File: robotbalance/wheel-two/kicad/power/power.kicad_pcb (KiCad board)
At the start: 2 copper layers, 55.9 x 35.6 mm, 0 parts

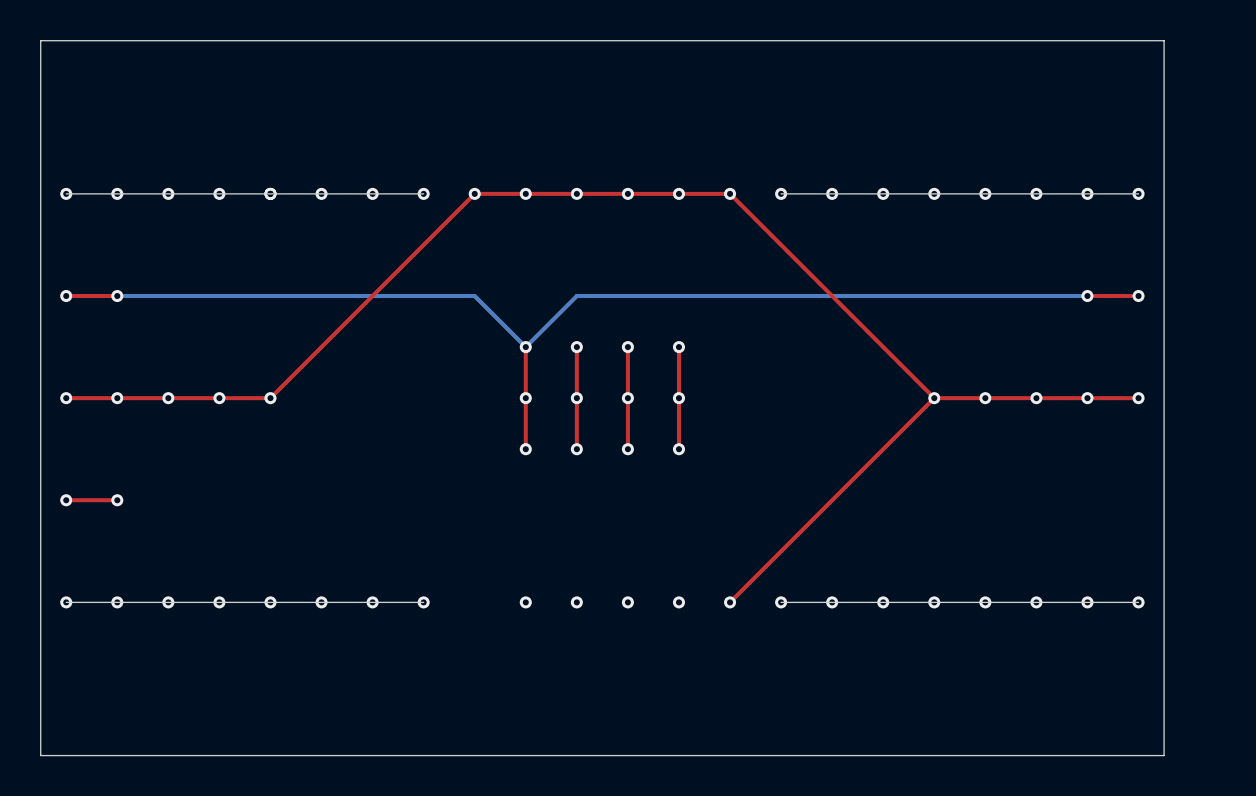
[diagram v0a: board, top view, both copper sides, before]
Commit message: balancing robot: 1.change pid in web in wifi 2.power board 3.another logic board esp32s3_weact+icm42688
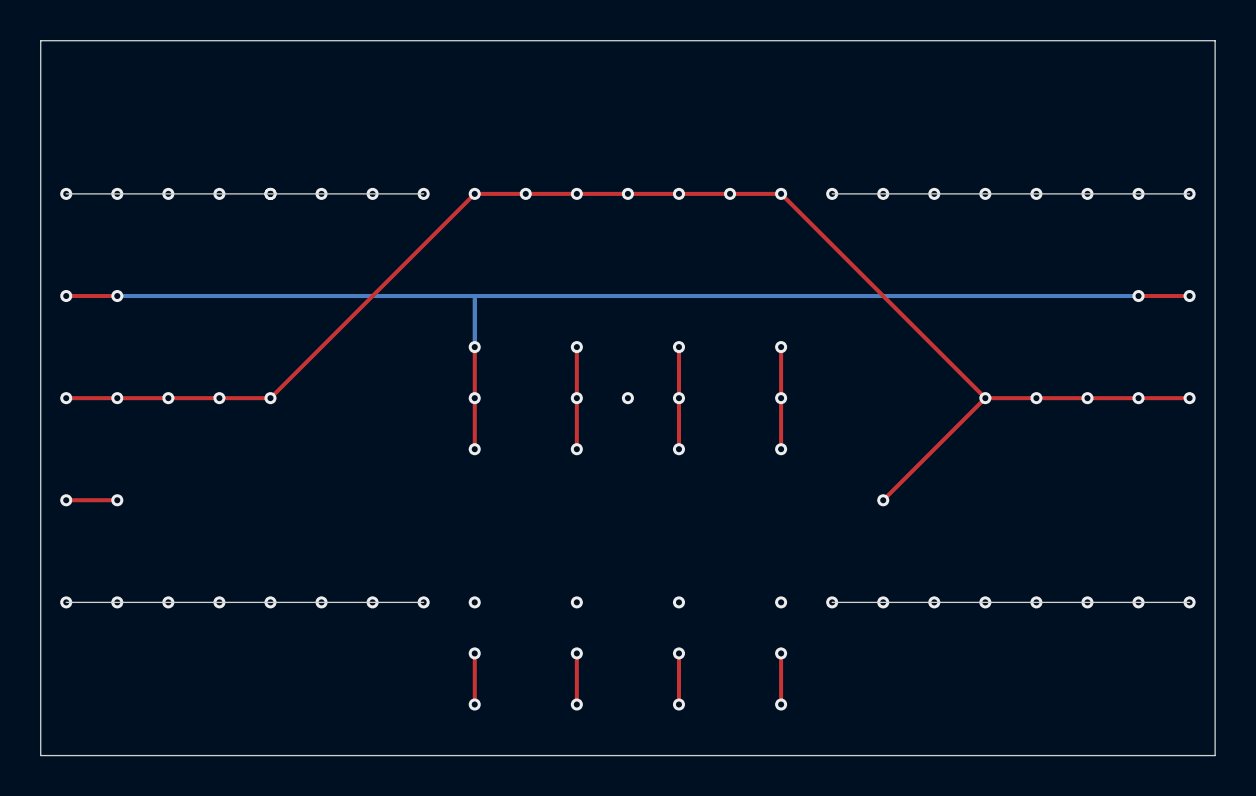
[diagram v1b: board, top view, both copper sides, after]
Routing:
- net (no net): track 154.4 -> 162.9 mm, vias 72 -> 82
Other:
- board size 55.9 x 35.6 mm -> 58.4 x 35.6 mm

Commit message: balancing robot: prepare for stepper motor
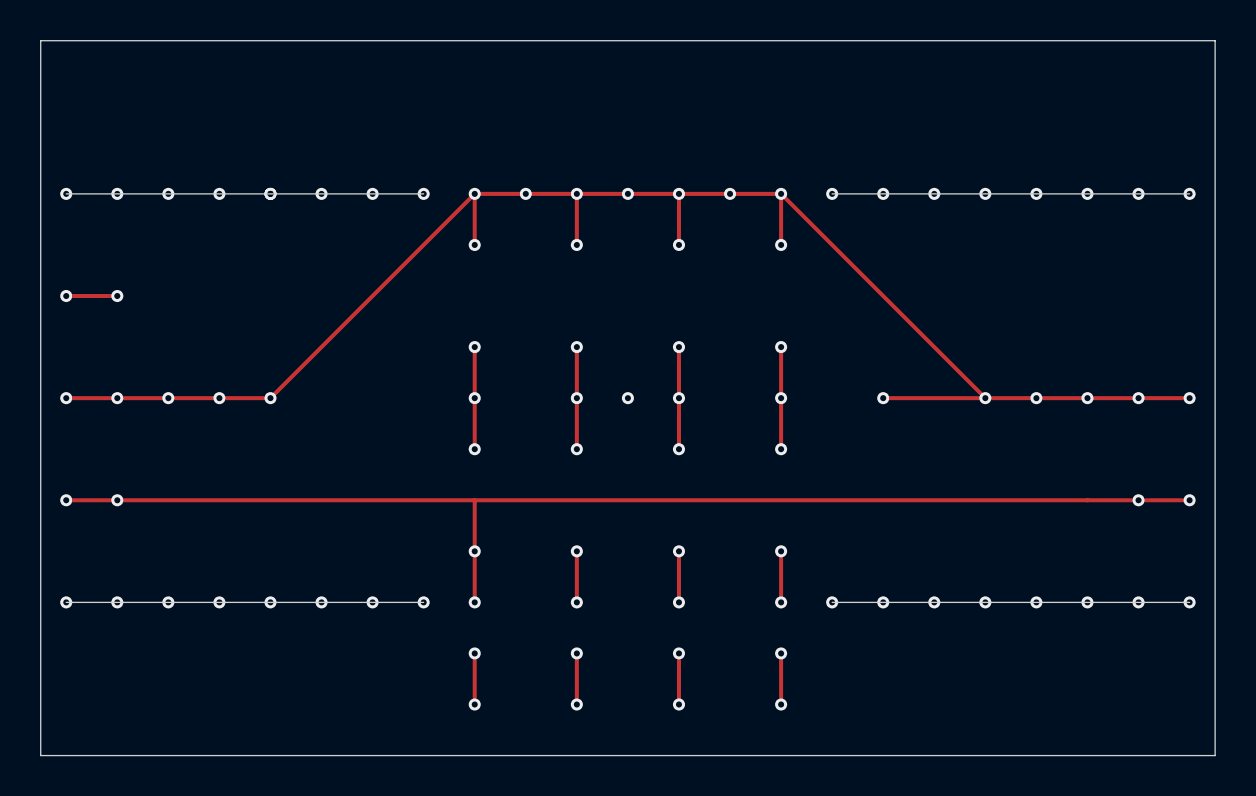
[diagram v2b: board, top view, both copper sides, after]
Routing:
- net (no net): track 162.9 -> 181.1 mm, vias 82 -> 90
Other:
- board text added: "gnd"
- board text removed: "0s"
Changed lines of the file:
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@@
 		)
 	)
-	(gr_text "4s"
-		(at 182.88 93.98 0)
-		(layer "Edge.Cuts")
-		(effects
-			(font
-				(size 1 1)
-				(thickness 0.15)
-			)
-			(justify right bottom)
-		)
-	)
-	(gr_text "0s"
-		(at 167.64 104.14 0)
+	(gr_text "gnd"
+		(at 167.64 99.06 0)
 		(layer "Edge.Cuts")
 		(effects
@@
 	)
 	(gr_text "4s"
-		(at 127 93.98 0)
+		(at 127 104.14 0)
 		(layer "Edge.Cuts")
 		(effects
@@
 	)
 	(gr_text "5v"
-		(at 127 104.14 0)
+		(at 127 93.98 0)
 		(layer "Edge.Cuts")
 		(effects
@@
 		)
 	)
+	(gr_text "4s"
+		(at 182.88 104.14 0)
+		(layer "Edge.Cuts")
+		(effects
+			(font
+				(size 1 1)
+				(thickness 0.15)
+			)
+			(justify right bottom)
+		)
+	)
 	(gr_text "3s"
 		(at 152.4 109.22 0)
@@
 	)
 	(segment
+		(start 162.56 106.68)
+		(end 162.56 109.22)
+		(width 0.2)
+		(layer "F.Cu")
+		(net 0)
+	)
+	(segment
+		(start 152.4 88.9)
+		(end 152.4 91.44)
+		(width 0.2)
+		(layer "F.Cu")
+		(net 0)
+	)
+	(segment
 		(start 147.32 88.9)
 		(end 137.16 99.06)
@@
 	)
 	(segment
+		(start 180.34 104.14)
+		(end 182.88 104.14)
+		(width 0.2)
+		(layer "F.Cu")
+		(net 0)
+	)
+	(segment
 		(start 172.72 99.06)
 		(end 175.26 99.06)
@@
 	)
 	(segment
+		(start 147.32 88.9)
+		(end 147.32 91.44)
+		(width 0.2)
+		(layer "F.Cu")
+		(net 0)
+	)
+	(segment
+		(start 147.32 104.14)
+		(end 147.32 106.68)
+		(width 0.2)
+		(layer "F.Cu")
+		(net 0)
+	)
+	(segment
+		(start 167.64 99.06)
+		(end 172.72 99.06)
+		(width 0.2)
+		(layer "F.Cu")
+		(net 0)
+	)
+	(segment
 		(start 157.48 111.76)
 		(end 157.48 114.3)
@@
 	)
 	(segment
+		(start 129.54 104.14)
+		(end 147.32 104.14)
+		(width 0.2)
+		(layer "F.Cu")
+		(net 0)
+	)
+	(segment
 		(start 134.62 99.06)
 		(end 132.08 99.06)
@@
 	)
 	(segment
+		(start 152.4 109.22)
+		(end 152.4 106.68)
+		(width 0.2)
+		(layer "F.Cu")
+		(net 0)
+	)
+	(segment
 		(start 152.4 111.76)
 		(end 152.4 114.3)
@@
 	)
 	(segment
-		(start 167.64 104.14)
-		(end 172.72 99.06)
-		(width 0.2)
-		(layer "F.Cu")
-		(net 0)
-	)
-	(segment
 		(start 180.34 99.06)
 		(end 182.88 99.06)
@@
 	)
 	(segment
+		(start 147.32 109.22)
+		(end 147.32 106.68)
+		(width 0.2)
+		(layer "F.Cu")
+		(net 0)
+	)
+	(segment
 		(start 149.86 88.9)
 		(end 147.32 88.9)
@@
 	)
 	(segment
-		(start 182.88 93.98)
-		(end 180.34 93.98)
+		(start 157.48 106.68)
+		(end 157.48 109.22)
 		(width 0.2)
 		(layer "F.Cu")
@@
 	)
 	(segment
+		(start 162.56 91.44)
+		(end 162.56 88.9)
+		(width 0.2)
+		(layer "F.Cu")
+		(net 0)
+	)
+	(segment
+		(start 147.32 104.14)
+		(end 177.8 104.14)
+		(width 0.2)
+		(layer "F.Cu")
+		(net 0)
+	)
+	(segment
 		(start 137.16 99.06)
 		(end 134.62 99.06)
@@
 	)
 	(segment
+		(start 157.48 91.44)
+		(end 157.48 88.9)
+		(width 0.2)
+		(layer "F.Cu")
+		(net 0)
+	)
+	(segment
+		(start 177.8 104.14)
+		(end 180.34 104.14)
+		(width 0.2)
+		(layer "F.Cu")
+		(net 0)
+	)
+	(segment
 		(start 172.72 99.06)
 		(end 162.56 88.9)
@@
 	)
 	(via
-		(at 167.64 104.14)
+		(at 167.64 99.06)
 		(size 0.6)
 		(drill 0.3)
@@
 	)
 	(via
+		(at 162.56 91.44)
+		(size 0.6)
+		(drill 0.3)
+		(layers "F.Cu" "B.Cu")
+		(net 0)
+	)
+	(via
 		(at 157.48 109.22)
 		(size 0.6)
@@
 	)
 	(via
+		(at 152.4 106.68)
+		(size 0.6)
+		(drill 0.3)
+		(layers "F.Cu" "B.Cu")
+		(net 0)
+	)
+	(via
 		(at 147.32 99.06)
 		(size 0.6)
@@
 	)
 	(via
+		(at 157.48 91.44)
+		(size 0.6)
+		(drill 0.3)
+		(layers "F.Cu" "B.Cu")
+		(net 0)
+	)
+	(via
 		(at 127 88.9)
 		(size 0.6)
@@
 	)
 	(via
+		(at 180.34 104.14)
+		(size 0.6)
+		(drill 0.3)
+		(layers "F.Cu" "B.Cu")
+		(net 0)
+	)
+	(via
+		(at 152.4 91.44)
+		(size 0.6)
+		(drill 0.3)
+		(layers "F.Cu" "B.Cu")
+		(net 0)
+	)
+	(via
 		(at 170.18 88.9)
 		(size 0.6)
@@
 	)
 	(via
+		(at 147.32 91.44)
+		(size 0.6)
+		(drill 0.3)
+		(layers "F.Cu" "B.Cu")
+		(net 0)
+	)
+	(via
 		(at 139.7 109.22)
 		(size 0.6)
@@
 	)
 	(via
+		(at 147.32 106.68)
+		(size 0.6)
+		(drill 0.3)
+		(layers "F.Cu" "B.Cu")
+		(net 0)
+	)
+	(via
 		(at 154.94 99.06)
 		(size 0.6)
@@
 	)
 	(via
-		(at 180.34 93.98)
-		(size 0.6)
-		(drill 0.3)
-		(layers "F.Cu" "B.Cu")
-		(net 0)
-	)
-	(via
 		(at 142.24 88.9)
 		(size 0.6)
@@
 	)
 	(via
+		(at 157.48 106.68)
+		(size 0.6)
+		(drill 0.3)
+		(layers "F.Cu" "B.Cu")
+		(net 0)
+	)
+	(via
 		(at 129.54 88.9)
 		(size 0.6)
@@
 	)
 	(via
+		(at 162.56 106.68)
+		(size 0.6)
+		(drill 0.3)
+		(layers "F.Cu" "B.Cu")
+		(net 0)
+	)
+	(via
 		(at 177.8 109.22)
 		(size 0.6)
@@
 	)
 	(via
+		(at 182.88 104.14)
+		(size 0.6)
+		(drill 0.3)
+		(layers "F.Cu" "B.Cu")
+		(net 0)
+	)
+	(via
 		(at 180.34 88.9)
 		(size 0.6)
@@
 	)
 	(via
-		(at 182.88 93.98)
-		(size 0.6)
-		(drill 0.3)
-		(layers "F.Cu" "B.Cu")
-		(net 0)
-	)
-	(via
 		(at 157.48 111.76)
 		(size 0.6)
@@
 		(net 0)
 	)
-	(segment
-		(start 147.32 93.98)
-		(end 129.54 93.98)
-		(width 0.2)
-		(layer "B.Cu")
-		(net 0)
-	)
-	(segment
-		(start 147.32 93.98)
-		(end 180.34 93.98)
-		(width 0.2)
-		(layer "B.Cu")
-		(net 0)
-	)
-	(segment
-		(start 147.32 96.52)
-		(end 147.32 93.98)
-		(width 0.2)
-		(layer "B.Cu")
-		(net 0)
-	)
